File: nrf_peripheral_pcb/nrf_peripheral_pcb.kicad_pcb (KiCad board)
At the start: 2 copper layers, 47 x 39.3 mm, 23 parts, among them U1 nRF52810-QCxx, U2 LIS2HH12, X1 32MHz

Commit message: pcb changes
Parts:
- moved BT1 16.4 mm to (134.9, 104.8), turned to 90 degrees
- moved JSWD1 7.57 mm to (144.2, 114.8)
- moved R1 4.30 mm to (129.3, 112.1)
- moved R2 4.30 mm to (129.3, 109.1)
- moved C11 4.30 mm to (123.7, 110.0)
- moved C12 4.30 mm to (123.7, 108.5)
- moved C14 4.30 mm to (123.8, 111.6)
- moved U2 4.30 mm to (127.3, 110.6)
- moved C15 2.98 mm to (137.5, 112.0), turned to 180 degrees
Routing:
- net VDD_nRF: track 0.00 -> 104.6 mm, vias 0 -> 6
- net GND: track 0.00 -> 62.8 mm, vias 0 -> 6
- net IMU_INT: track 0.00 -> 14.8 mm, vias 0 -> 2
- net SDA: track 0.00 -> 8.87 mm
- net Net-(JSWD1-Pad2): track 0.00 -> 8.29 mm
- net Net-(X1-Pad2): track 0.00 -> 7.49 mm
- net Net-(X1-Pad1): track 0.00 -> 7.08 mm
- net Net-(JSWD1-Pad3): track 0.00 -> 7.00 mm
- net Net-(L3-Pad1): track 0.00 -> 6.88 mm
- net Net-(L3-Pad2): track 0.00 -> 5.77 mm
- net Net-(L1-Pad2): track 0.00 -> 3.29 mm
- net Net-(C7-Pad2): track 0.00 -> 2.99 mm
- net Net-(C4-Pad1): track 0.00 -> 1.95 mm
- net Net-(L2-Pad2): track 0.00 -> 1.36 mm
- added copper zone on B.Cu, net GND
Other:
- board size 47 x 39.3 mm -> 37.1 x 37.1 mm

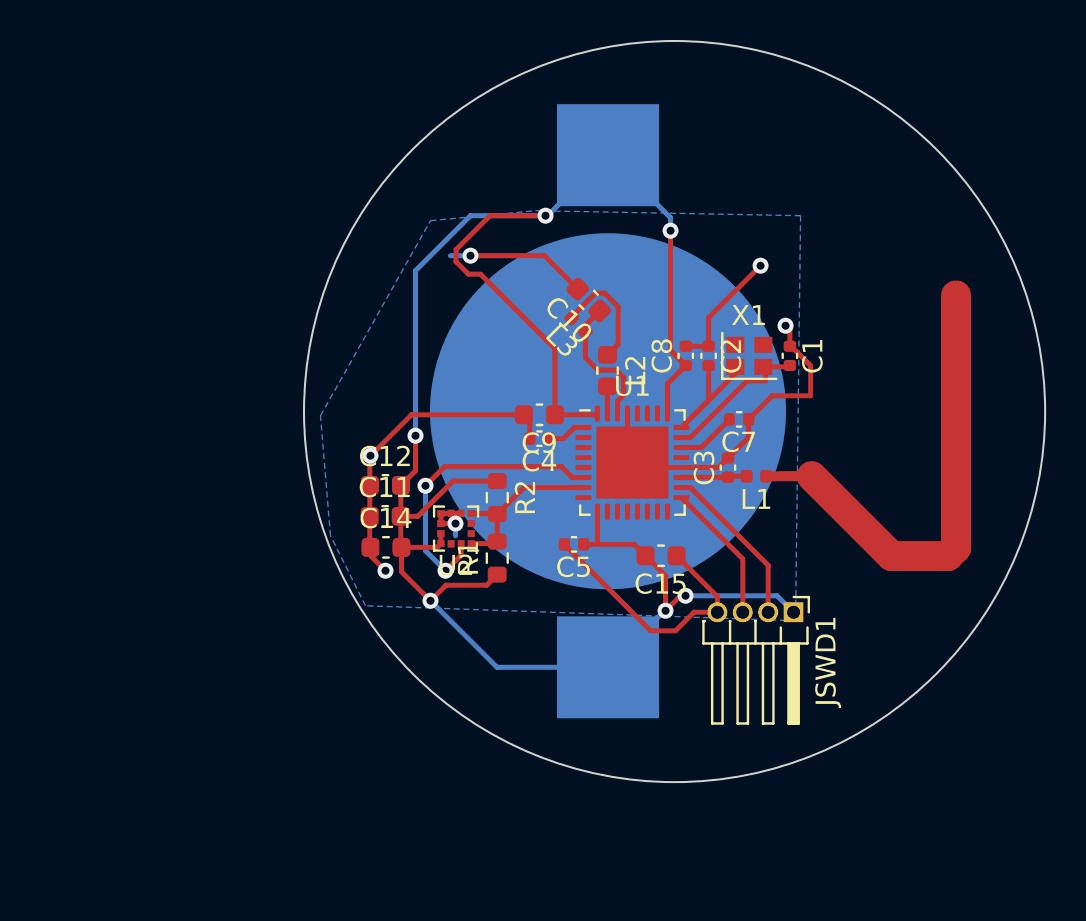
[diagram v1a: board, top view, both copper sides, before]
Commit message: changed pcb size
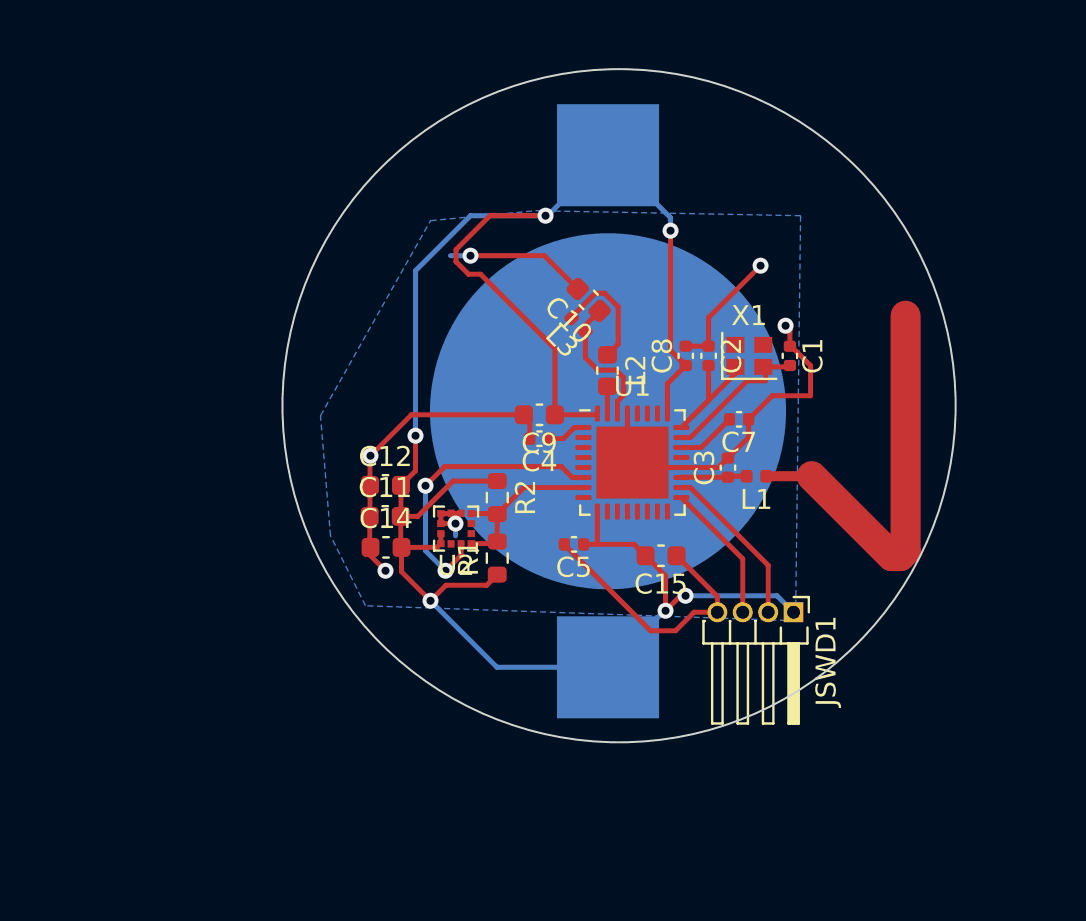
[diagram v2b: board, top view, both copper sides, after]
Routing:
- net unconnected-(L1-Pad1): track 23.9 -> 20.5 mm
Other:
- board size 37.1 x 37.1 mm -> 33.7 x 33.7 mm
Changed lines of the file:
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@@
     )
   )
-  (gr_circle (center 138.2014 104.791825) (end 156.718 104.228217) (layer "Edge.Cuts") (width 0.1) (fill none))
+  (gr_circle (center 135.425363 104.5) (end 152.25 104.25) (layer "Edge.Cuts") (width 0.1) (fill none))
   (segment (start 140.860791 107.1144) (end 140.384791 107.5904) (width 0.25) (layer "F.Cu") (net 1))
   (segment (start 131.6964 97) (end 128 97) (width 0.25) (layer "F.Cu") (net 1))
@@
   (segment (start 141.61 112.1572) (end 138.5432 109.0904) (width 0.25) (layer "F.Cu") (net 10))
   (segment (start 141.61 114.825) (end 141.61 112.1572) (width 0.25) (layer "F.Cu") (net 10))
+  (segment (start 149.5 112) (end 149.75 111.75) (width 1.5) (layer "F.Cu") (net 11))
   (segment (start 142.7758 108.0262) (end 145.056072 108.019129) (width 0.5) (layer "F.Cu") (net 11))
-  (segment (start 152.273 111.6076) (end 152.273 98.9838) (width 1.5) (layer "F.Cu") (net 11))
-  (segment (start 151.8666 112.014) (end 152.273 111.6076) (width 1.5) (layer "F.Cu") (net 11))
+  (segment (start 149.486 112.014) (end 149.5 112) (width 1.5) (layer "F.Cu") (net 11))
+  (segment (start 149.75 111.75) (end 149.75 100) (width 1.5) (layer "F.Cu") (net 11))
   (segment (start 145.056072 108.019129) (end 149.050943 112.014) (width 1.5) (layer "F.Cu") (net 11))
-  (segment (start 149.050943 112.014) (end 151.8666 112.014) (width 1.5) (layer "F.Cu") (net 11))
+  (segment (start 149.050943 112.014) (end 149.486 112.014) (width 1.5) (layer "F.Cu") (net 11))
   (segment (start 133.057853 100.114053) (end 133.057853 100.063347) (width 0.25) (layer "F.Cu") (net 12))
   (segment (start 134.246668 98.874532) (end 134.702304 98.874532) (width 0.25) (layer "F.Cu") (net 12))
